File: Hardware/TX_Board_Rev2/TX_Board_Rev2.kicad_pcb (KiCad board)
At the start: 4 copper layers, 104.9 x 89.8 mm, 311 parts, among them IC1 GP2Y1+, IC2 GP2Y1+, IC3 GP2Y1+, J0 CONSMA022-G, J1 CONSMA022-G, J10 MM8030-2610RJ3, J11 MM8030-2610RJ3, J18 Conn_01x08, J19 694106301002, J2 CONSMA022-G, J3 CONSMA022-G, J4 MM8030-2610RJ3, J5 MM8030-2610RJ3, J6 MM8030-2610RJ3, J7 MM8030-2610RJ3, J8 MM8030-2610RJ3, J9 MM8030-2610RJ3, SW00 PE42423B-Z, SW01 PE42423B-Z, SW10 PE42423B-Z, SW11 PE42423B-Z, SW20 PE42423B-Z, SW21 PE42423B-Z, SW30 PE42423B-Z, SW31 PE42423B-Z, U1 SN74HCT138NSR

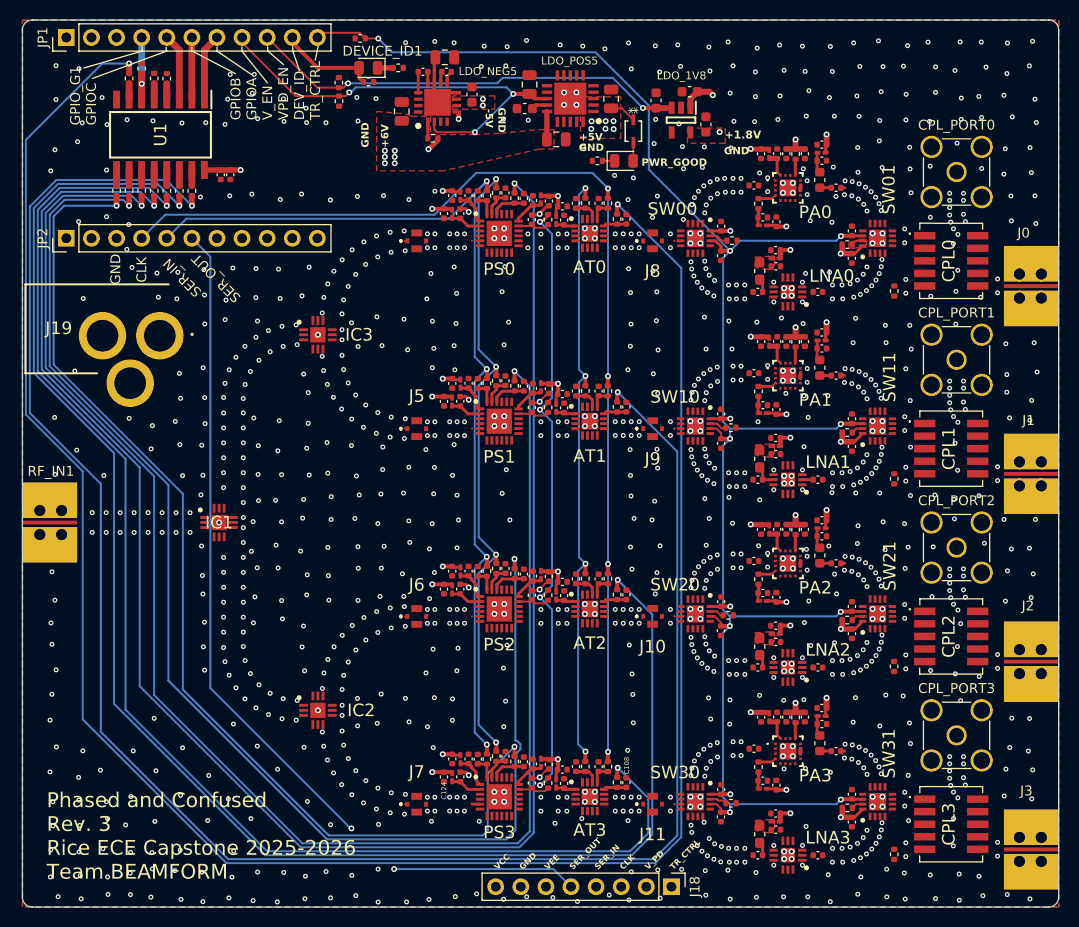
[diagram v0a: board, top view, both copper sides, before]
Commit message: Restored broken Rev 2 for posterity and cleaned up naming
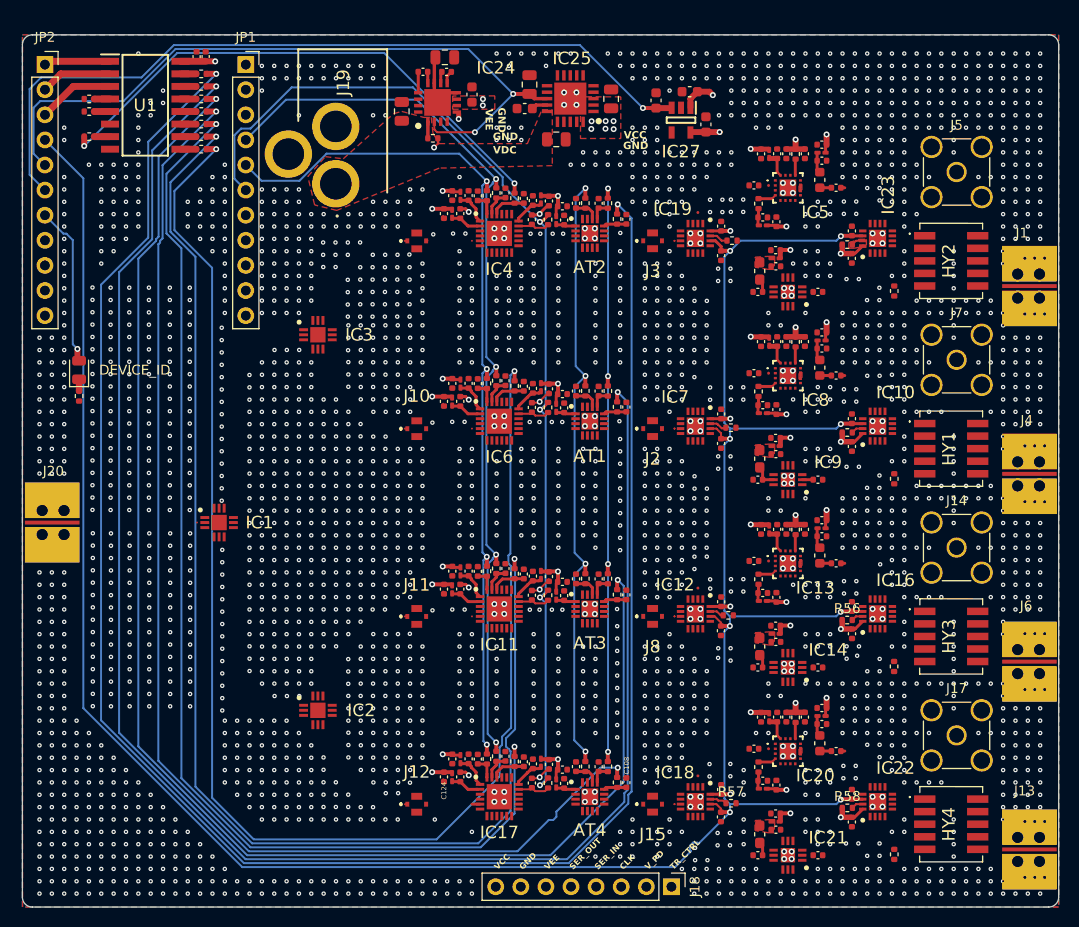
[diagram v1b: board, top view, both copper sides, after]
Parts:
- removed APT2012LSECK/J3-PRV1, DEVICE_ID1: LED, LED_SMD:LED_0805_2012Metric
- removed CR1: BZT52C2V4S-7-F, BZT52C2V4S_7_F:SOD323_DIO
- removed R61, R62, R63, R65, R66: 100k, Resistor_SMD:R_0402_1005Metric
- removed R64: 300, Resistor_SMD:R_0402_1005Metric
- added DEVICE_ID: LED, LED_SMD:LED_0805_2012Metric, F.Cu at (105.4, 88.7)
- JP1, JP2: footprint Connector_PinHeader_2.54mm:PinHeader_1x11_P2.54mm_Vertical -> Connector_PinSocket_2.54mm:PinSocket_1x11_P2.54mm_Vertical
- moved R60 46.3 mm to (105.4, 91.3), turned to -90 degrees
- moved J19 42.9 mm to (127.6, 56.2), turned to -90 degrees
- moved JP1 18.4 mm to (122.3, 57.8), turned to 0 degrees
- moved JP2 17.7 mm to (102.0, 57.8), turned to 0 degrees
- moved C4 12.2 mm to (118.2, 56.9), turned to -90 degrees
- moved C5 12.2 mm to (117.3, 56.9), turned to -90 degrees
- moved R5 11.9 mm to (117.8, 58.7), turned to 0 degrees
- moved R6 10.8 mm to (117.8, 60.0), turned to 0 degrees
- moved R7 9.92 mm to (117.8, 61.2), turned to 0 degrees
- moved R11 9.55 mm to (117.8, 66.3), turned to 0 degrees
- moved R8 9.33 mm to (117.8, 62.5), turned to 0 degrees
- moved R10 9.13 mm to (117.8, 65.0), turned to 0 degrees
- moved R9 9.05 mm to (117.8, 63.8), turned to 0 degrees
- moved R1 8.11 mm to (106.4, 61.2), turned to 0 degrees
- moved R2 7.38 mm to (106.4, 62.5), turned to 0 degrees
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- renumbered AT0 to AT2, AT2 to AT3, AT3 to AT4, CPL1 to HY1, CPL0 to HY2, CPL2 to HY3, CPL3 to HY4, SW11 to IC10, PS2 to IC11, SW20 to IC12, PA2 to IC13, LNA2 to IC14, LNA0 to IC15, SW21 to IC16, PS3 to IC17, SW30 to IC18, SW00 to IC19, PA3 to IC20, LNA3 to IC21, SW31 to IC22, SW01 to IC23, LDO_NEG5 to IC24, LDO_POS5 to IC25, LDO_1V8 to IC27, PS0 to IC4, PA0 to IC5, PS1 to IC6, SW10 to IC7, PA1 to IC8, LNA1 to IC9, J0 to J1, J5 to J10, J6 to J11, J7 to J12, J3 to J13, CPL_PORT2 to J14, J11 to J15, CPL_PORT3 to J17, J9 to J2, RF_IN1 to J20, J8 to J3, J1 to J4, CPL_PORT0 to J5, J2 to J6, CPL_PORT1 to J7, J10 to J8, J4 to J9
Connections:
- JP1 pad 1: GND -> unconnected-(JP1-Pad1)
- JP1 pad 10: DEVICE_ID -> unconnected-(JP1-Pad10)
- JP1 pad 11: TR_CTRL -> unconnected-(JP1-Pad11)
- JP1 pad 3: unconnected-(JP1-Pad3) -> GND
- JP1 pad 4: GPIO-G1 -> CLK
- JP1 pad 5: GPIOC -> SER_IN
- JP1 pad 6: GPIOB -> SER_OUT
- JP1 pad 7: GPIOA -> unconnected-(JP1-Pad7)
- JP1 pad 8: V_EN -> unconnected-(JP1-Pad8)
- JP1 pad 9: VPD_EN -> unconnected-(JP1-Pad9)
- JP2 pad 1: unconnected-(JP2-Pad1) -> GPIO1
- JP2 pad 2: unconnected-(JP2-Pad2) -> GPIO2
- JP2 pad 3: GND -> GPIO3
- JP2 pad 4: CLK -> TR_CTRL
- JP2 pad 5: SER_IN -> V_EN
- JP2 pad 6: SER_OUT -> VPD_EN
- JP2 pad 7: unconnected-(JP2-Pad7) -> DEVICE_ID
- R11 pad 2: PS_LE_3 -> PS_LE_1
- R3 pad 1: ATTN_LE_0 -> PS_LE_0
- R5 pad 2: ATTN_LE_1 -> ATTN_LE_0
- R6 pad 2: ATTN_LE_2 -> ATTN_LE_1
- R7 pad 2: ATTN_LE_3 -> ATTN_LE_2
- R8 pad 2: PS_LE_0 -> ATTN_LE_3
- R9 pad 2: PS_LE_1 -> PS_LE_3
- U1 pad 1: GPIOA -> GPIO1
- U1 pad 2: GPIOB -> GPIO2
- U1 pad 3: GPIOC -> GPIO3
- U1 pad 6: GPIO-G1 -> GPIO0
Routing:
- net PS_LE_0: track 180.7 -> 54.9 mm
- net TR_CTRL: track 189.4 -> 268.2 mm, vias 9 -> 8
- net VDC: track 62.0 -> 1.81 mm, vias 6 -> 0
- net SER_OUT: track 167.5 -> 119.8 mm, vias 6 -> 4
- net VPD_EN: track 45.5 -> 80.3 mm, vias 2 -> 1
- net V_EN: track 45.5 -> 73.3 mm, vias 3 -> 2
- net CLK: track 203.1 -> 180.8 mm
- net ATTN_LE_1: track 188.7 -> 172.3 mm
- net ATTN_LE_0: track 211.0 -> 195.4 mm
- net VCC: track 102.3 -> 87.5 mm
- net ATTN_LE_3: track 138.5 -> 124.2 mm
- net ATTN_LE_2: track 161.1 -> 148.2 mm
- net PS_LE_1: track 158.1 -> 146.2 mm
- net SER_IN: track 187.5 -> 179.0 mm
- net GPIO3: track 0.00 -> 7.78 mm
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- removed copper zone on In2.Cu, net VDC
- removed copper zone on F.Cu, net V_PD
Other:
- board size 104.9 x 89.8 mm -> 104.9 x 88.2 mm
- board text added: "VDC"
- board text removed: "+1.8V"
- board text removed: "+5V"
- board text removed: "+6V"
- board text removed: "-5V"
- board text removed: "8=D~"
- board text removed: "Designed By: Big Hoff Tommy Pickle ERAW Jushashasha Con"
- board text removed: "GPIOB GPIOA V_EN VPD_EN DEV_ID TR_CTRL"
- board text removed: "GPIO_G1 GPIOC"
- board text removed: "PCB3D_BR_TX_Board_Rev3"
- board text removed: "PCB3D_TL_TX_Board_Rev3"
- board text removed: "PWR_GOOD"
- board text removed: "Phased and Confused Rev. 3 Rice ECE Capstone 2025-2026 Team BEAMFORM"
